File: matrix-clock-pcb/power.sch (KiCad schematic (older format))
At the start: 18 parts

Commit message: pcb: update pcb files
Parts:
- J3: renamed from J?; footprint (none) -> Connector_PinHeader_2.54mm:PinHeader_1x02_P2.54mm_Vertical
- gave numbers to parts that had none: 17
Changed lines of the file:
@@
 AR Path="/5F232324" Ref="#PWR?"  Part="1"
 AR Path="/5F2186C0/5F232324" Ref="#PWR?"  Part="1"
-AR Path="/5F4ECFED/5F232324" Ref="#PWR?"  Part="1"
-F 0 "#PWR?" H 1250 3300 50  0001 C CNN
+AR Path="/5F4ECFED/5F232324" Ref="#PWR0123"  Part="1"
+F 0 "#PWR0123" H 1250 3300 50  0001 C CNN
 F 1 "GND" H 1255 3377 50  0000 C CNN
 F 2 "" H 1250 3550 50  0001 C CNN
@@
 Connection ~ 1250 3550
 $Comp
-L Connector:USB_C_Receptacle_USB2.0 J?
+L Connector:USB_C_Receptacle_USB2.0 J4
 U 1 1 5F4D6B71
 P 1550 2650
-F 0 "J?" H 1657 3517 50  0000 C CNN
+F 0 "J4" H 1657 3517 50  0000 C CNN
 F 1 "USB_C_Receptacle_USB2.0" H 1657 3426 50  0000 C CNN
 F 2 "Connector_USB:USB_C_Receptacle_HRO_TYPE-C-31-M-12" H 1700 2650 50  0001 C CNN
@@
 AR Path="/5F24A068" Ref="U?"  Part="1"
 AR Path="/5F2186C0/5F24A068" Ref="U?"  Part="1"
-AR Path="/5F4ECFED/5F24A068" Ref="U?"  Part="1"
-F 0 "U?" H 3950 5792 50  0000 C CNN
+AR Path="/5F4ECFED/5F24A068" Ref="U5"  Part="1"
+F 0 "U5" H 3950 5792 50  0000 C CNN
 F 1 "AMS1117-3.3" H 3950 5701 50  0000 C CNN
 F 2 "Package_TO_SOT_SMD:SOT-223-3_TabPin2" H 3950 5750 50  0001 C CNN
@@
 AR Path="/5F24A06E" Ref="#PWR?"  Part="1"
 AR Path="/5F2186C0/5F24A06E" Ref="#PWR?"  Part="1"
-AR Path="/5F4ECFED/5F24A06E" Ref="#PWR?"  Part="1"
-F 0 "#PWR?" H 4650 5400 50  0001 C CNN
+AR Path="/5F4ECFED/5F24A06E" Ref="#PWR0124"  Part="1"
+F 0 "#PWR0124" H 4650 5400 50  0001 C CNN
 F 1 "+3.3V" V 4650 5800 50  0000 C CNN
 F 2 "" H 4650 5550 50  0001 C CNN
@@
 AR Path="/5F24A075" Ref="#PWR?"  Part="1"
 AR Path="/5F2186C0/5F24A075" Ref="#PWR?"  Part="1"
-AR Path="/5F4ECFED/5F24A075" Ref="#PWR?"  Part="1"
-F 0 "#PWR?" H 3950 5600 50  0001 C CNN
+AR Path="/5F4ECFED/5F24A075" Ref="#PWR0125"  Part="1"
+F 0 "#PWR0125" H 3950 5600 50  0001 C CNN
 F 1 "GND" H 3955 5677 50  0000 C CNN
 F 2 "" H 3950 5850 50  0001 C CNN
@@
 AR Path="/5F24A081" Ref="C?"  Part="1"
 AR Path="/5F2186C0/5F24A081" Ref="C?"  Part="1"
-AR Path="/5F4ECFED/5F24A081" Ref="C?"  Part="1"
-F 0 "C?" H 3615 5746 50  0000 L CNN
+AR Path="/5F4ECFED/5F24A081" Ref="C7"  Part="1"
+F 0 "C7" H 3615 5746 50  0000 L CNN
 F 1 "10uf" H 3615 5655 50  0000 L CNN
 F 2 "Capacitor_SMD:C_0805_2012Metric" H 3538 5550 50  0001 C CNN
@@
 AR Path="/5F24A087" Ref="C?"  Part="1"
 AR Path="/5F2186C0/5F24A087" Ref="C?"  Part="1"
-AR Path="/5F4ECFED/5F24A087" Ref="C?"  Part="1"
-F 0 "C?" H 4565 5746 50  0000 L CNN
+AR Path="/5F4ECFED/5F24A087" Ref="C9"  Part="1"
+F 0 "C9" H 4565 5746 50  0000 L CNN
 F 1 "10uf" H 4565 5655 50  0000 L CNN
 F 2 "Capacitor_SMD:C_0805_2012Metric" H 4488 5550 50  0001 C CNN
@@
 	3500 5850 3950 5850
 $Comp
-L Interface_USB:CP2102N-A01-GQFN28 U?
+L Interface_USB:CP2102N-A01-GQFN28 U6
 U 1 1 5F567655
 P 5150 3250
-F 0 "U?" H 4800 1950 50  0000 C CNN
+F 0 "U6" H 4800 1950 50  0000 C CNN
 F 1 "CP2102N-A01-GQFN28" H 5700 1950 50  0000 C CNN
 F 2 "Package_DFN_QFN:QFN-28-1EP_5x5mm_P0.5mm_EP3.35x3.35mm" H 5600 2050 50  0001 L CNN
@@
 $EndComp
 $Comp
-L Device:R R?
+L Device:R R7
 U 1 1 5F56C1C8
 P 4450 2100
-F 0 "R?" H 4350 2050 50  0000 C CNN
+F 0 "R7" H 4350 2050 50  0000 C CNN
 F 1 "10K" H 4350 1950 50  0000 C CNN
 F 2 "Resistor_SMD:R_0402_1005Metric" V 4380 2100 50  0001 C CNN
@@
 $EndComp
 $Comp
-L Device:R R?
+L Device:R R8
 U 1 1 5F5762E2
 P 6600 2650
-F 0 "R?" V 6393 2650 50  0000 C CNN
+F 0 "R8" V 6393 2650 50  0000 C CNN
 F 1 "10K" V 6484 2650 50  0000 C CNN
 F 2 "Resistor_SMD:R_0402_1005Metric" V 6530 2650 50  0001 C CNN
@@
 $EndComp
 $Comp
-L Device:R R?
+L Device:R R9
 U 1 1 5F57697D
 P 6600 3250
-F 0 "R?" V 6393 3250 50  0000 C CNN
+F 0 "R9" V 6393 3250 50  0000 C CNN
 F 1 "10K" V 6484 3250 50  0000 C CNN
 F 2 "Resistor_SMD:R_0402_1005Metric" V 6530 3250 50  0001 C CNN
@@
 AR Path="/5F5A892F" Ref="#PWR?"  Part="1"
 AR Path="/5F2186C0/5F5A892F" Ref="#PWR?"  Part="1"
-AR Path="/5F4ECFED/5F5A892F" Ref="#PWR?"  Part="1"
-F 0 "#PWR?" H 5150 4300 50  0001 C CNN
+AR Path="/5F4ECFED/5F5A892F" Ref="#PWR0126"  Part="1"
+F 0 "#PWR0126" H 5150 4300 50  0001 C CNN
 F 1 "GND" H 5155 4377 50  0000 C CNN
 F 2 "" H 5150 4550 50  0001 C CNN
@@
 AR Path="/5F5A9CF0" Ref="C?"  Part="1"
 AR Path="/5F2186C0/5F5A9CF0" Ref="C?"  Part="1"
-AR Path="/5F4ECFED/5F5A9CF0" Ref="C?"  Part="1"
-F 0 "C?" H 4400 2250 50  0000 C CNN
+AR Path="/5F4ECFED/5F5A9CF0" Ref="C8"  Part="1"
+F 0 "C8" H 4400 2250 50  0000 C CNN
 F 1 "1uf" H 4400 2350 50  0000 C CNN
 F 2 "Capacitor_SMD:C_0603_1608Metric" H 4288 2250 50  0001 C CNN
@@
 AR Path="/5F5AB474" Ref="C?"  Part="1"
 AR Path="/5F2186C0/5F5AB474" Ref="C?"  Part="1"
-AR Path="/5F4ECFED/5F5AB474" Ref="C?"  Part="1"
-F 0 "C?" V 5250 2000 50  0000 L CNN
+AR Path="/5F4ECFED/5F5AB474" Ref="C10"  Part="1"
+F 0 "C10" V 5250 2000 50  0000 L CNN
 F 1 "0.1uf" V 5150 1850 50  0000 L CNN
 F 2 "Capacitor_SMD:C_0402_1005Metric" H 5338 1750 50  0001 C CNN
@@
 AR Path="/5F5ADB3F" Ref="#PWR?"  Part="1"
 AR Path="/5F2186C0/5F5ADB3F" Ref="#PWR?"  Part="1"
-AR Path="/5F4ECFED/5F5ADB3F" Ref="#PWR?"  Part="1"
-F 0 "#PWR?" H 5450 1650 50  0001 C CNN
+AR Path="/5F4ECFED/5F5ADB3F" Ref="#PWR0127"  Part="1"
+F 0 "#PWR0127" H 5450 1650 50  0001 C CNN
 F 1 "GND" H 5455 1727 50  0000 C CNN
 F 2 "" H 5450 1900 50  0001 C CNN
@@
 AR Path="/5F5B107E" Ref="#PWR?"  Part="1"
 AR Path="/5F2186C0/5F5B107E" Ref="#PWR?"  Part="1"
-AR Path="/5F4ECFED/5F5B107E" Ref="#PWR?"  Part="1"
-F 0 "#PWR?" H 4250 2000 50  0001 C CNN
+AR Path="/5F4ECFED/5F5B107E" Ref="#PWR0128"  Part="1"
+F 0 "#PWR0128" H 4250 2000 50  0001 C CNN
 F 1 "GND" H 4255 2077 50  0000 C CNN
 F 2 "" H 4250 2250 50  0001 C CNN
@@
 	2150 2650 2150 2550
 $Comp
-L Device:R R?
+L Device:R R5
 U 1 1 5F524A26
 P 3000 2450
-F 0 "R?" V 3100 2550 50  0000 C CNN
+F 0 "R5" V 3100 2550 50  0000 C CNN
 F 1 "22" V 3100 2400 50  0000 C CNN
 F 2 "Resistor_SMD:R_0402_1005Metric" V 2930 2450 50  0001 C CNN
@@
 $EndComp
 $Comp
-L Device:R R?
+L Device:R R6
 U 1 1 5F525525
 P 3000 2650
-F 0 "R?" V 3100 2750 50  0000 C CNN
+F 0 "R6" V 3100 2750 50  0000 C CNN
 F 1 "22" V 3100 2600 50  0000 C CNN
 F 2 "Resistor_SMD:R_0402_1005Metric" V 2930 2650 50  0001 C CNN
@@
 	2750 2650 2750 2750
 $Comp
-L Transistor_BJT:MMBT5551L Q?
+L Transistor_BJT:MMBT5551L Q1
 U 1 1 5FA32740
 P 6950 2650
-F 0 "Q?" H 7141 2696 50  0000 L CNN
+F 0 "Q1" H 7141 2696 50  0000 L CNN
 F 1 "MMBT5551L" H 7141 2605 50  0000 L CNN
 F 2 "Package_TO_SOT_SMD:SOT-23" H 7150 2575 50  0001 L CIN
@@
 $EndComp
 $Comp
-L Transistor_BJT:MMBT5551L Q?
+L Transistor_BJT:MMBT5551L Q2
 U 1 1 5FA3811B
 P 6950 3250
-F 0 "Q?" H 7141 3204 50  0000 L CNN
+F 0 "Q2" H 7141 3204 50  0000 L CNN
 F 1 "MMBT5551L" H 7141 3295 50  0000 L CNN
 F 2 "Package_TO_SOT_SMD:SOT-23" H 7150 3175 50  0001 L CIN
@@
 	7050 3450 7350 3450
 $Comp
-L power:VBUS #PWR?
+L power:VBUS #PWR0129
 U 1 1 5FA3C304
 P 2250 2050
-F 0 "#PWR?" H 2250 1900 50  0001 C CNN
+F 0 "#PWR0129" H 2250 1900 50  0001 C CNN
 F 1 "VBUS" V 2265 2178 50  0000 L CNN
 F 2 "" H 2250 2050 50  0001 C CNN
@@
 $EndComp
 $Comp
-L power:VBUS #PWR?
+L power:VBUS #PWR0130
 U 1 1 5FA3C75A
 P 4050 2550
-F 0 "#PWR?" H 4050 2400 50  0001 C CNN
+F 0 "#PWR0130" H 4050 2400 50  0001 C CNN
 F 1 "VBUS" V 4065 2677 50  0000 L CNN
 F 2 "" H 4050 2550 50  0001 C CNN
@@
 $EndComp
 $Comp
-L power:VBUS #PWR?
+L power:VBUS #PWR0131
 U 1 1 5FA3C991
 P 5050 1950
-F 0 "#PWR?" H 5050 1800 50  0001 C CNN
+F 0 "#PWR0131" H 5050 1800 50  0001 C CNN
 F 1 "VBUS" H 5065 2123 50  0000 C CNN
 F 2 "" H 5050 1950 50  0001 C CNN
@@
 $EndComp
 $Comp
-L Diode:1N4148WS D?
+L Diode:1N4148WS D3
 U 1 1 5FA51EAF
 P 3100 5150
-F 0 "D?" H 3100 4933 50  0000 C CNN
+F 0 "D3" H 3100 4933 50  0000 C CNN
 F 1 "1N4148WS" H 3100 5024 50  0000 C CNN
 F 2 "Diode_SMD:D_SOD-323" H 3100 4975 50  0001 C CNN
@@
 $EndComp
 $Comp
-L Diode:1N4148WS D?
+L Diode:1N4148WS D4
 U 1 1 5FA531EA
 P 3100 5550
-F 0 "D?" H 3200 5600 50  0000 C CNN
+F 0 "D4" H 3200 5600 50  0000 C CNN
 F 1 "1N4148WS" H 3100 5700 50  0000 C CNN
 F 2 "Diode_SMD:D_SOD-323" H 3100 5375 50  0001 C CNN
@@
 	3250 5550 3500 5550
 $Comp
-L power:VBUS #PWR?
+L power:VBUS #PWR0132
 U 1 1 5FA553E7
 P 2600 5150
-F 0 "#PWR?" H 2600 5000 50  0001 C CNN
+F 0 "#PWR0132" H 2600 5000 50  0001 C CNN
 F 1 "VBUS" V 2615 5277 50  0000 L CNN
 F 2 "" H 2600 5150 50  0001 C CNN
@@
 $EndComp
 $Comp
-L power:+5V #PWR?
+L power:+5V #PWR0133
 U 1 1 5FA5674E
 P 2600 5550
-F 0 "#PWR?" H 2600 5400 50  0001 C CNN
+F 0 "#PWR0133" H 2600 5400 50  0001 C CNN
 F 1 "+5V" V 2615 5678 50  0000 L CNN
 F 2 "" H 2600 5550 50  0001 C CNN
@@
 $EndComp
 $Comp
-L Diode:1N4148WS D?
+L Diode:1N4148WS D2
 U 1 1 5FA573BE
 P 2800 5300
-F 0 "D?" V 2891 5220 50  0000 R CNN
+F 0 "D2" V 2891 5220 50  0000 R CNN
 F 1 "1N4148WS" V 2800 5220 50  0000 R CNN
 F 2 "Diode_SMD:D_SOD-323" H 2800 5125 50  0001 C CNN
@@
 	2800 5550 2950 5550
 $Comp
-L Connector_Generic:Conn_01x02 J?
+L Connector_Generic:Conn_01x02 J3
 U 1 1 5FA635CD
 P 1250 4750
-F 0 "J?" H 1168 4425 50  0000 C CNN
+F 0 "J3" H 1168 4425 50  0000 C CNN
 F 1 "Conn_01x02" H 1168 4516 50  0000 C CNN
-F 2 "" H 1250 4750 50  0001 C CNN
+F 2 "Connector_PinHeader_2.54mm:PinHeader_1x02_P2.54mm_Vertical" H 1250 4750 50  0001 C CNN
 F 3 "~" H 1250 4750 50  0001 C CNN
 	1    1250 4750
@@
 $EndComp
 $Comp
-L power:+5V #PWR?
+L power:+5V #PWR0134
 U 1 1 5FA64DD9
 P 1450 4650
-F 0 "#PWR?" H 1450 4500 50  0001 C CNN
+F 0 "#PWR0134" H 1450 4500 50  0001 C CNN
 F 1 "+5V" V 1465 4778 50  0000 L CNN
 F 2 "" H 1450 4650 50  0001 C CNN
@@
 AR Path="/5FA65831" Ref="#PWR?"  Part="1"
 AR Path="/5F2186C0/5FA65831" Ref="#PWR?"  Part="1"
-AR Path="/5F4ECFED/5FA65831" Ref="#PWR?"  Part="1"
-F 0 "#PWR?" H 1450 4500 50  0001 C CNN
+AR Path="/5F4ECFED/5FA65831" Ref="#PWR0135"  Part="1"
+F 0 "#PWR0135" H 1450 4500 50  0001 C CNN
 F 1 "GND" H 1455 4577 50  0000 C CNN
 F 2 "" H 1450 4750 50  0001 C CNN

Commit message: fix(pcb): modify cp2102 IO voltage to 3.3v; add ir receiver
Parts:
- added R?: 24k, Resistor_SMD:R_0402_1005Metric, symbol Device:R
- added R?: 47k, Resistor_SMD:R_0402_1005Metric, symbol Device:R
- C10: value 0.1uf -> 1uf
- C8: footprint Capacitor_SMD:C_0603_1608Metric -> Capacitor_SMD:C_0402_1005Metric
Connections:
- net GND: now also C10.2, C8.1, R?.2; no longer C10.1, C8.2
- net VBUS: now also C10.1, R?.1; no longer C8.1, U6.8 (VBUS)
- net at R7.2, U6.6 (VDD): now also C8.2; no longer C10.2
- new net: R?.1, R?.2, U6.8 (VBUS)

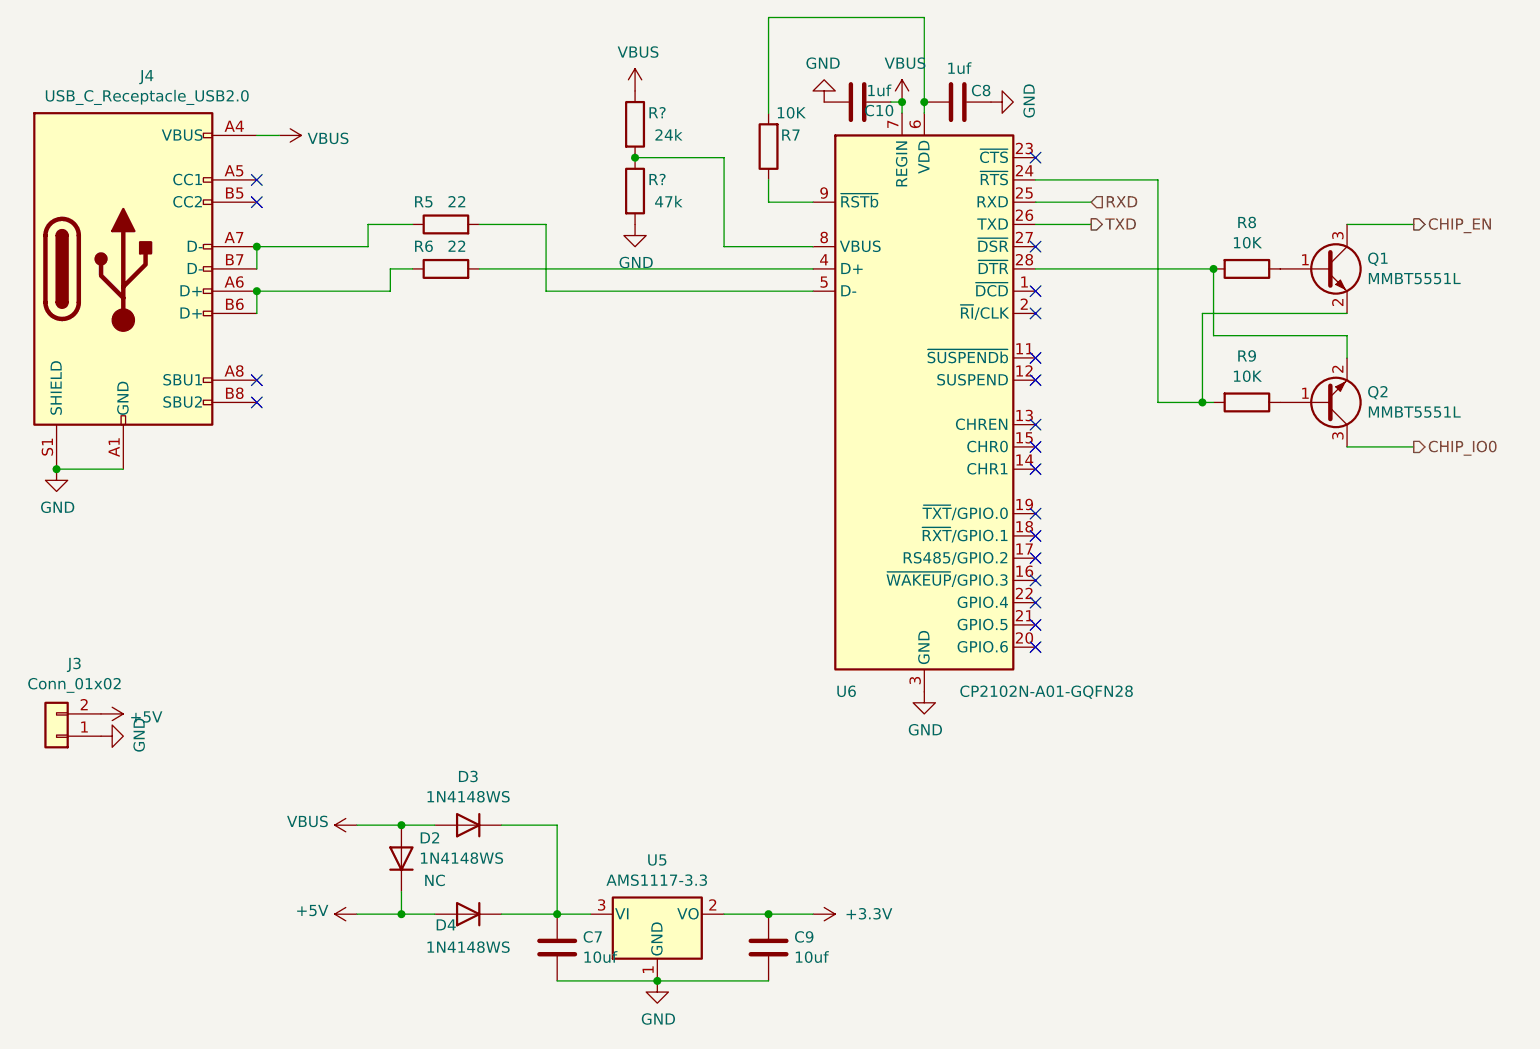
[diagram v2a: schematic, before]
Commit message: fix(pcb): update pcb layout
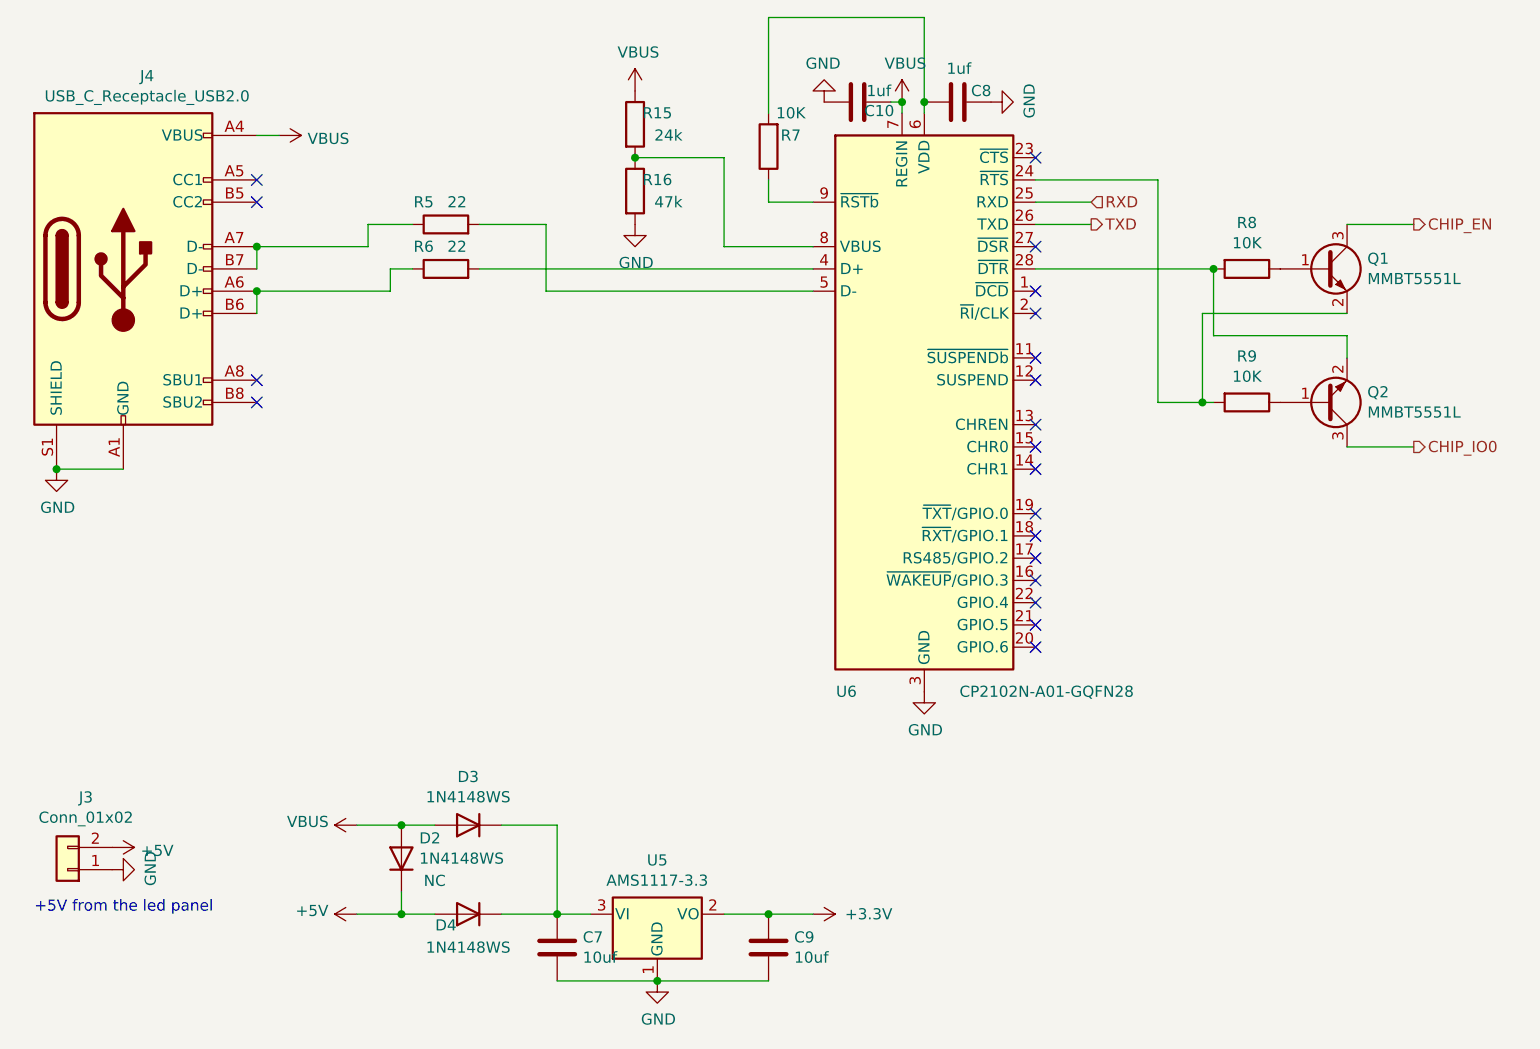
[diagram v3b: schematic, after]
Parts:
- gave numbers to parts that had none: 2
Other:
- note added: "+5V from the led panel"
- moved on the sheet: J3
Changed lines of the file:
@@
 $Descr A4 11693 8268
 encoding utf-8
-Sheet 2 3
+Sheet 3 3
 Title "power"
 Date "2020-09-01"
@@
 L Connector_Generic:Conn_01x02 J3
 U 1 1 5FA635CD
-P 1250 4750
-F 0 "J3" H 1168 4425 50  0000 C CNN
-F 1 "Conn_01x02" H 1168 4516 50  0000 C CNN
-F 2 "Connector_PinHeader_2.54mm:PinHeader_1x02_P2.54mm_Vertical" H 1250 4750 50  0001 C CNN
-F 3 "~" H 1250 4750 50  0001 C CNN
-	1    1250 4750
+P 1300 5350
+F 0 "J3" H 1218 5025 50  0000 C CNN
+F 1 "Conn_01x02" H 1218 5116 50  0000 C CNN
+F 2 "Connector_PinHeader_2.54mm:PinHeader_1x02_P2.54mm_Vertical" H 1300 5350 50  0001 C CNN
+F 3 "~" H 1300 5350 50  0001 C CNN
+	1    1300 5350
 	-1   0    0    1
 $EndComp
@@
 L power:+5V #PWR0134
 U 1 1 5FA64DD9
-P 1450 4650
-F 0 "#PWR0134" H 1450 4500 50  0001 C CNN
-F 1 "+5V" V 1465 4778 50  0000 L CNN
-F 2 "" H 1450 4650 50  0001 C CNN
-F 3 "" H 1450 4650 50  0001 C CNN
-	1    1450 4650
+P 1500 5250
+F 0 "#PWR0134" H 1500 5100 50  0001 C CNN
+F 1 "+5V" V 1515 5378 50  0000 L CNN
+F 2 "" H 1500 5250 50  0001 C CNN
+F 3 "" H 1500 5250 50  0001 C CNN
+	1    1500 5250
 	0    1    1    0
 $EndComp
@@
 L power:GND #PWR?
 U 1 1 5FA65831
-P 1450 4750
+P 1500 5350
 AR Path="/5FA65831" Ref="#PWR?"  Part="1"
 AR Path="/5F2186C0/5FA65831" Ref="#PWR?"  Part="1"
 AR Path="/5F4ECFED/5FA65831" Ref="#PWR0135"  Part="1"
-F 0 "#PWR0135" H 1450 4500 50  0001 C CNN
-F 1 "GND" H 1455 4577 50  0000 C CNN
-F 2 "" H 1450 4750 50  0001 C CNN
-F 3 "" H 1450 4750 50  0001 C CNN
-	1    1450 4750
+F 0 "#PWR0135" H 1500 5100 50  0001 C CNN
+F 1 "GND" H 1505 5177 50  0000 C CNN
+F 2 "" H 1500 5350 50  0001 C CNN
+F 3 "" H 1500 5350 50  0001 C CNN
+	1    1500 5350
 	0    -1   -1   0
 $EndComp
 $Comp
-L Device:R R?
+L Device:R R15
 U 1 1 604532E6
 P 3850 2000
-F 0 "R?" H 3950 2050 50  0000 C CNN
+F 0 "R15" H 3950 2050 50  0000 C CNN
 F 1 "24k" H 4000 1950 50  0000 C CNN
 F 2 "Resistor_SMD:R_0402_1005Metric" V 3780 2000 50  0001 C CNN
@@
 $EndComp
 $Comp
-L Device:R R?
+L Device:R R16
 U 1 1 604536C3
 P 3850 2300
-F 0 "R?" H 3950 2350 50  0000 C CNN
+F 0 "R16" H 3950 2350 50  0000 C CNN
 F 1 "47k" H 4000 2250 50  0000 C CNN
 F 2 "Resistor_SMD:R_0402_1005Metric" V 3780 2300 50  0001 C CNN
@@
 $EndComp
 $Comp
-L power:VBUS #PWR?
+L power:VBUS #PWR05
 U 1 1 6045C76C
 P 3850 1850
-F 0 "#PWR?" H 3850 1700 50  0001 C CNN
+F 0 "#PWR05" H 3850 1700 50  0001 C CNN
 F 1 "VBUS" H 3865 2023 50  0000 C CNN
 F 2 "" H 3850 1850 50  0001 C CNN
@@
 AR Path="/604670C0" Ref="#PWR?"  Part="1"
 AR Path="/5F2186C0/604670C0" Ref="#PWR?"  Part="1"
-AR Path="/5F4ECFED/604670C0" Ref="#PWR?"  Part="1"
-F 0 "#PWR?" H 4700 1650 50  0001 C CNN
+AR Path="/5F4ECFED/604670C0" Ref="#PWR06"  Part="1"
+F 0 "#PWR06" H 4700 1650 50  0001 C CNN
 F 1 "GND" H 4705 1727 50  0000 C CNN
 F 2 "" H 4700 1900 50  0001 C CNN
@@
 Data
 89 50 4E 47 0D 0A 1A 0A 00 00 00 0D 49 48 44 52 00 00 03 41 00 00 02 5D 08 02 00 00 00 7B FC EB
-DA 00 00 00 03 73 42 49 54 08 08 08 DB E1 4F E0 00 00 00 09 70 48 59 73 00 00 0E C3 00 00 0E C3
-01 C7 6F A8 64 00 00 20 00 49 44 41 54 78 9C EC 9D 79 BC 5D 45 95 EF 7F 35 EC E1 CC 77 CC 4D 72
+DA 00 00 00 03 73 42 49 54 08 08 08 DB E1 4F E0 00 00 00 09 70 48 59 73 00 00 0E 74 00 00 0E 74
+01 6B 24 B3 D6 00 00 20 00 49 44 41 54 78 9C EC 9D 79 BC 5D 45 95 EF 7F 35 EC E1 CC 77 CC 4D 72
 13 90 21 1D 95 20 20 93 88 10 81 A0 84 19 04 A2 A0 A2 B4 03 D8 E2 F0 50 5A 44 69 F5 D1 A0 A8 D8
 4E 2D 0D 68 3B 00 6A B7 20 34 E2 6C 00 65 E8 7E 34 08 8A 08 08 12 86 4C DC F9 4C 7B AE 7A 7F AC
@@
 	5150 1520 5150 1900
 Connection ~ 5150 1900
+Text Notes 1150 5550 0    50   ~ 0
++5V from the led panel
 $EndSCHEMATC
